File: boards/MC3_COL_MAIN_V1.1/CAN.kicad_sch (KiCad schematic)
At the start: 11 parts, among them J12 CAN, U8 TJA1051T/3

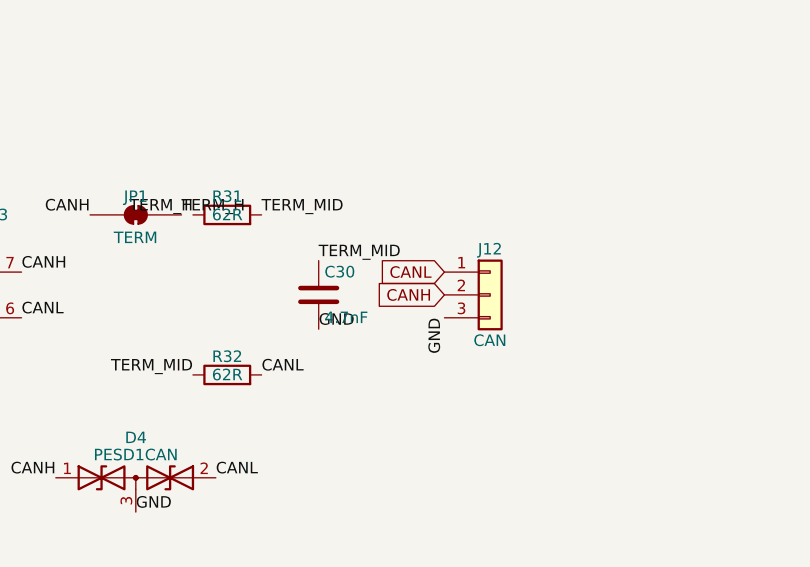
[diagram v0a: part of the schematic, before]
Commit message: V1.1: encoder FFC VIN on filtered VSENS, motor pads off MotorChannel, yaw nets renamed
- Connectors: encoder FFC VIN now fed from VSENS (VM through FB61 + C63);
  ENC_leaf1-4 / RC_OUT labels re-placed; SIG pull-ups to +3V3 noted on sheet
- MotorChannel: J7-J9 MOTOR pad connectors (Conn_01x02) and their OUT1/OUT2
  hierarchical labels removed from the shared sheet
- MCU: ENC_leaf1-4 global labels re-placed; sheet notes carried over
- Root: H5 SLOT-PASSTHRU mounting hole removed
- PCB: yaw motor nets YAW_OUT* -> /yaw/OUT*; CANH/CANL pad assignment swapped;
  VSENS/VM net reassignments and follow-up routing (~106 segments, 12 vias,
  zone edits) to match the schematic

Co-Authored-By: Claude Fable 5 <noreply@anthropic.com>
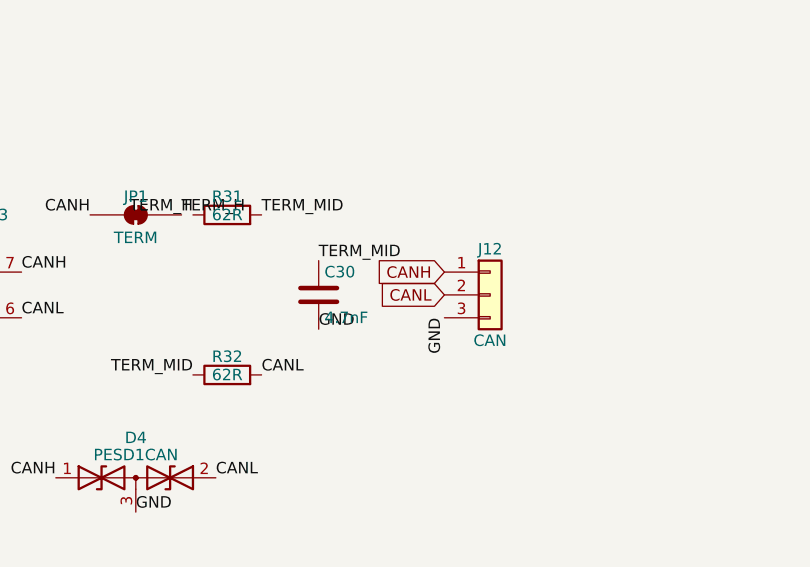
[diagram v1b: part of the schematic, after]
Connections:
- net CANH: now also J12.1 (Pin_1); no longer J12.2 (Pin_2)
- net CANL: now also J12.2 (Pin_2); no longer J12.1 (Pin_1)
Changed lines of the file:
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@@
 		)
 	)
-	(global_label "CANL"
+	(global_label "CANH"
 		(shape input)
 		(at 160.02 77.47 180)
@@
 		)
 	)
-	(global_label "CANH"
+	(global_label "CANL"
 		(shape input)
 		(at 160.02 80.01 180)

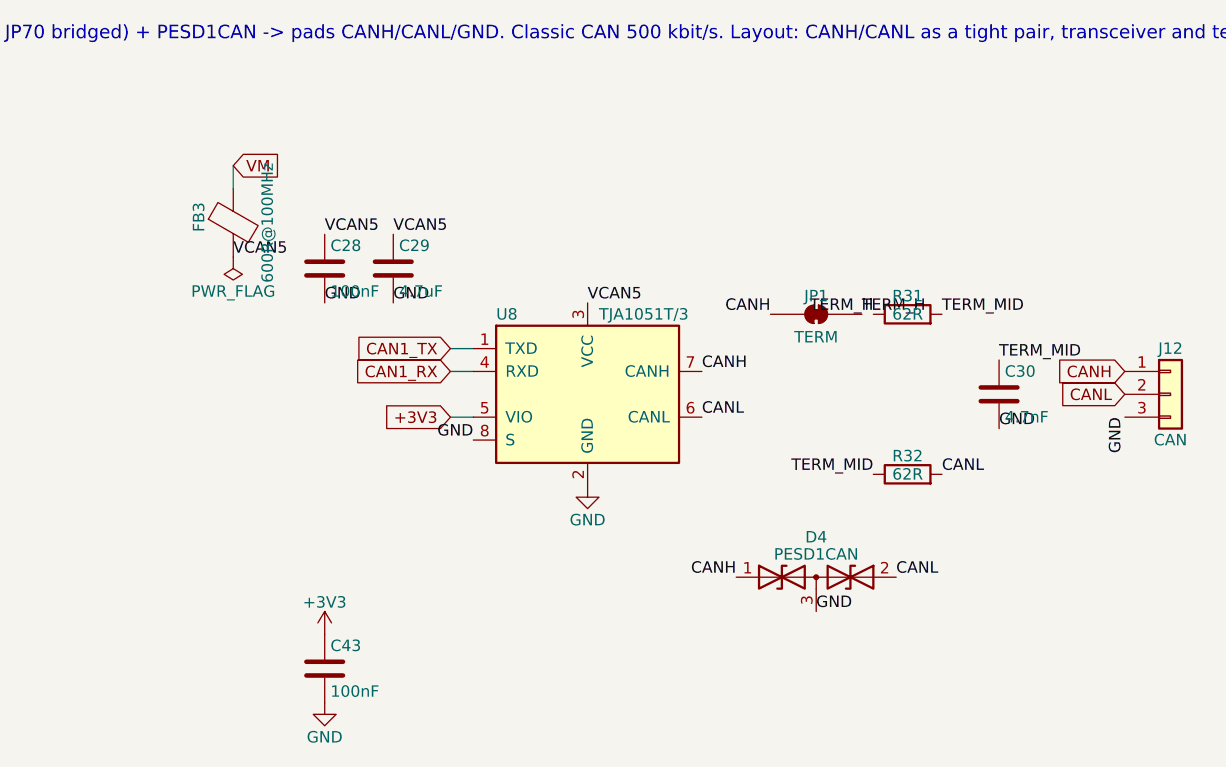
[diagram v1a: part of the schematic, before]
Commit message: Vault consolidation: Main-Board-02 rung folded back into Main-Board-01
Nothing was built at V1.0, so the 24 V revision never justified a rung bump.
Main-Board-01 now builds boards/MC3_COL_MAIN_V1.1 (24 V input); V1.0 stays in
the repo as the 5 V-only fallback revision. Repo side: CLAUDE.md rung mapping,
MIGRATION.md header and §14 pointer, LM61460 layout-note link. Vault side
(edited directly): Main-Board-01 Power rewritten as the 24 V chain, rung page
carries the V1.0→V1.1 delta/BOM/gates, Main-Board-02 folder deleted, 13 pages'
references rewritten.

Co-Authored-By: Claude Fable 5 <noreply@anthropic.com>
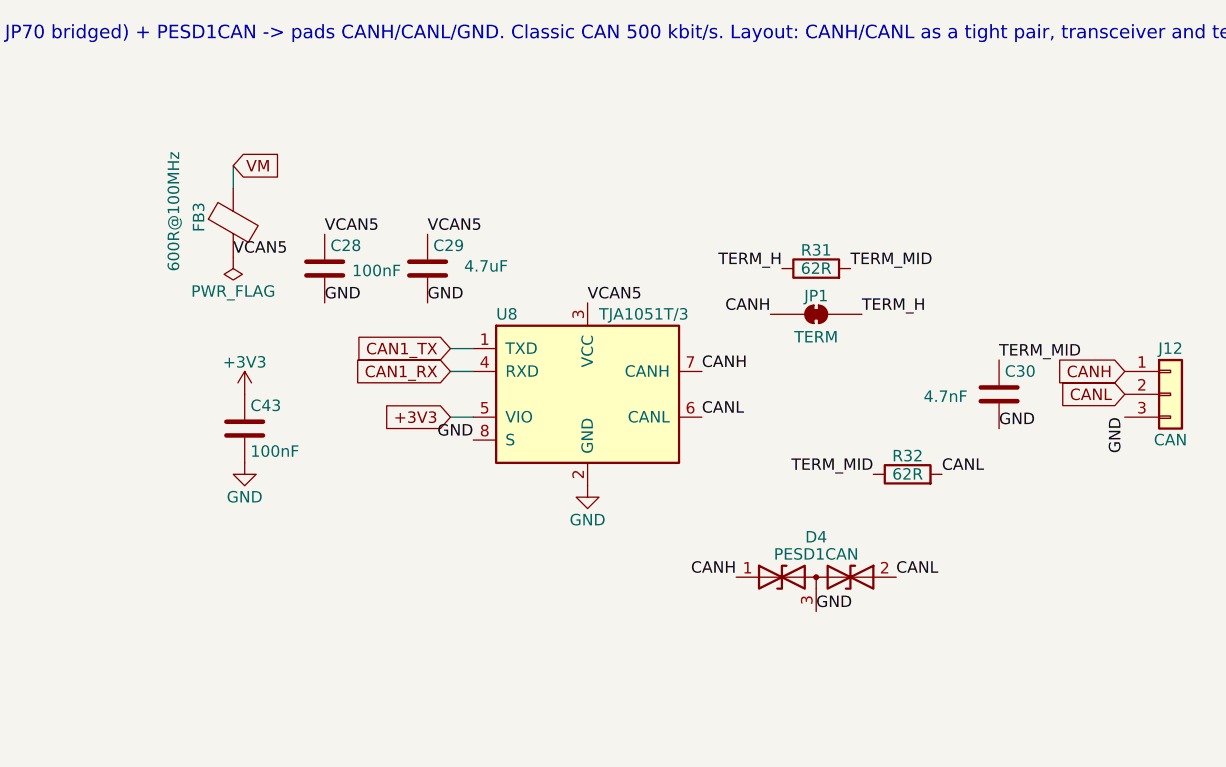
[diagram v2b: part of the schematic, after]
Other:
- moved on the sheet: C29, C43, R31
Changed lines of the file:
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@@
 	)
 	(label "TERM_MID"
-		(at 139.7 71.12 0)
+		(at 129.54 66.04 0)
 		(effects
 			(font
@@
 	)
 	(label "GND"
-		(at 78.74 69.85 0)
+		(at 82.55 69.85 0)
 		(effects
 			(font
@@
 	)
 	(label "TERM_H"
-		(at 132.08 71.12 180)
+		(at 121.92 66.04 180)
 		(effects
 			(font
@@
 	)
 	(label "VCAN5"
-		(at 78.74 62.23 0)
+		(at 82.55 62.23 0)
 		(effects
 			(font
@@
 	(symbol
 		(lib_id "power:+3V3")
-		(at 71.12 106.68 0)
+		(at 62.23 80.01 0)
 		(unit 1)
 		(body_style 1)
@@
 		(dnp no)
 		(property "Reference" "#PWR0120"
-			(at 71.12 110.49 0)
+			(at 62.23 83.82 0)
 			(hide yes)
 			(show_name no)
@@
 		)
 		(property "Value" "+3V3"
-			(at 71.12 103.124 0)
+			(at 62.23 76.454 0)
 			(show_name no)
 			(do_not_autoplace no)
@@
 		)
 		(property "Footprint" ""
-			(at 71.12 106.68 0)
+			(at 62.23 80.01 0)
 			(hide yes)
 			(show_name no)
@@
 		)
 		(property "Datasheet" ""
-			(at 71.12 106.68 0)
+			(at 62.23 80.01 0)
 			(hide yes)
 			(show_name no)
@@
 		)
 		(property "Description" ""
-			(at 71.12 106.68 0)
+			(at 62.23 80.01 0)
 			(show_name no)
 			(do_not_autoplace no)
@@
 		)
 		(property "Value" "100nF"
-			(at 71.755 68.58 0)
+			(at 74.168 66.294 0)
 			(show_name no)
 			(do_not_autoplace no)
@@
 	(symbol
 		(lib_id "Device:C")
-		(at 78.74 66.04 0)
+		(at 82.55 66.04 0)
 		(unit 1)
 		(body_style 1)
@@
 		(dnp no)
 		(property "Reference" "C29"
-			(at 79.375 63.5 0)
+			(at 83.185 63.5 0)
 			(show_name no)
 			(do_not_autoplace no)
@@
 		)
 		(property "Value" "4.7uF"
-			(at 79.375 68.58 0)
+			(at 86.614 65.786 0)
 			(show_name no)
 			(do_not_autoplace no)
@@
 		)
 		(property "Footprint" "MC3_COL_MAIN:C_0603_1608Metric"
-			(at 78.74 66.04 0)
+			(at 82.55 66.04 0)
 			(hide yes)
 			(show_name no)
@@
 		)
 		(property "Datasheet" ""
-			(at 78.74 66.04 0)
+			(at 82.55 66.04 0)
 			(hide yes)
 			(show_name no)
@@
 		)
 		(property "Description" ""
-			(at 78.74 66.04 0)
+			(at 82.55 66.04 0)
 			(show_name no)
 			(do_not_autoplace no)
@@
 		)
 		(property "LCSC" "C19666"
-			(at 78.74 66.04 0)
+			(at 82.55 66.04 0)
 			(hide yes)
 			(show_name no)
@@
 		)
 		(property "MPN" "CL10A475KO8NNNC"
-			(at 78.74 66.04 0)
+			(at 82.55 66.04 0)
 			(hide yes)
 			(show_name no)
@@
 	(symbol
 		(lib_id "power:GND")
-		(at 71.12 114.3 0)
+		(at 62.23 87.63 0)
 		(unit 1)
 		(body_style 1)
@@
 		(dnp no)
 		(property "Reference" "#PWR0121"
-			(at 71.12 120.65 0)
+			(at 62.23 93.98 0)
 			(hide yes)
 			(show_name no)
@@
 		)
 		(property "Value" "GND"
-			(at 71.12 118.11 0)
+			(at 62.23 91.44 0)
 			(show_name no)
 			(do_not_autoplace no)
@@
 		)
 		(property "Footprint" ""
-			(at 71.12 114.3 0)
+			(at 62.23 87.63 0)
 			(hide yes)
 			(show_name no)
@@
 		)
 		(property "Datasheet" ""
-			(at 71.12 114.3 0)
+			(at 62.23 87.63 0)
 			(hide yes)
 			(show_name no)
@@
 		)
 		(property "Description" ""
-			(at 71.12 114.3 0)
+			(at 62.23 87.63 0)
 			(show_name no)
 			(do_not_autoplace no)
@@
 	(symbol
 		(lib_id "Device:C")
-		(at 71.12 110.49 0)
+		(at 62.23 83.82 0)
 		(unit 1)
 		(body_style 1)
@@
 		(dnp no)
 		(property "Reference" "C43"
-			(at 71.755 107.95 0)
+			(at 62.865 81.28 0)
 			(show_name no)
 			(do_not_autoplace no)
@@
 		)
 		(property "Value" "100nF"
-			(at 71.755 113.03 0)
+			(at 62.865 86.36 0)
 			(show_name no)
 			(do_not_autoplace no)
@@
 		)
 		(property "Footprint" "MC3_COL_MAIN:C_0402_1005Metric"
-			(at 71.12 110.49 0)
+			(at 62.23 83.82 0)
 			(hide yes)
 			(show_name no)
@@
 		)
 		(property "Datasheet" ""
-			(at 71.12 110.49 0)
+			(at 62.23 83.82 0)
 			(hide yes)
 			(show_name no)
@@
 		)
 		(property "Description" ""
-			(at 71.12 110.49 0)
+			(at 62.23 83.82 0)
 			(show_name no)
 			(do_not_autoplace no)
@@
 		)
 		(property "LCSC" "C1525"
-			(at 71.12 110.49 0)
+			(at 62.23 83.82 0)
 			(hide yes)
 			(show_name no)
@@
 		)
 		(property "Note" "U8 VIO (pin 5) local decoupling - place within 4 mm of pin 5; wire pin1 to +3V3, pin2 to GND"
-			(at 71.12 110.49 0)
+			(at 62.23 83.82 0)
 			(hide yes)
 			(show_name no)
@@
 		)
 		(property "Value" "600R@100MHz"
-			(at 64.77 60.96 90)
+			(at 54.356 59.69 90)
 			(show_name no)
 			(do_not_autoplace no)
@@
 	(symbol
 		(lib_id "Device:R")
-		(at 135.89 71.12 90)
+		(at 125.73 66.04 90)
 		(unit 1)
 		(body_style 1)
@@
 		(dnp no)
 		(property "Reference" "R31"
-			(at 135.89 69.088 90)
+			(at 125.73 64.008 90)
 			(show_name no)
 			(do_not_autoplace no)
@@
 		)
 		(property "Value" "62R"
-			(at 135.89 71.12 90)
+			(at 125.73 66.04 90)
 			(show_name no)
 			(do_not_autoplace no)
@@
 		)
 		(property "Footprint" "MC3_COL_MAIN:R_0402_1005Metric"
-			(at 135.89 71.12 0)
+			(at 125.73 66.04 0)
 			(hide yes)
 			(show_name no)
@@
 		)
 		(property "Datasheet" ""
-			(at 135.89 71.12 0)
+			(at 125.73 66.04 0)
 			(hide yes)
 			(show_name no)
@@
 		)
 		(property "Description" ""
-			(at 135.89 71.12 0)
+			(at 125.73 66.04 0)
 			(show_name no)
 			(do_not_autoplace no)
@@
 		)
 		(property "LCSC" "C4962"
-			(at 135.89 71.12 0)
+			(at 125.73 66.04 0)
 			(hide yes)
 			(show_name no)
@@
 		)
 		(property "MPN" "0402WGF620JTCE"
-			(at 135.89 71.12 0)
+			(at 125.73 66.04 0)
 			(hide yes)
 			(show_name no)
@@
 		)
 		(property "Note" "Split termination 62R+62R (~124R) with C72 4.7nF to GND; JP70 bridged = terminated (board is a bus end on the bench). Cut JP70 if the board sits mid-bus in the machine"
-			(at 135.89 71.12 0)
+			(at 125.73 66.04 0)
 			(hide yes)
 			(show_name no)
@@
 		)
 		(property "Value" "4.7nF"
-			(at 146.685 82.55 0)
-			(show_name no)
-			(do_not_autoplace no)
+			(at 137.668 80.264 0)
+			(show_name no)
+			(do_not_autoplace no)

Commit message: V1.1 schematics: per-instance Description fields on ~63 symbols
The component-docs Role source of record. Netlist unchanged, ERC 0.

Co-Authored-By: Claude Fable 5 <noreply@anthropic.com>
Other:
- note removed: "CAN - machine control link (decision 2026-08-22; vault Control Electronics open item). STM32F412 CAN1 (PA11 RX / PA12 TX) -> TJA1051T/3 -> split termination (2x62R + 4.7nF, solder-jumper JP70 bridged) + PESD1CAN -> pads CANH/CANL/GND. Classic CAN 500 kbit/s. Layout: CANH/CANL as a tight pair, transceiver and termination next to the pads, D70 nearest the pads."
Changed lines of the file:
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@@
 	(generator_version "10.0")
 	(paper "A4")
-	(text "CAN - machine control link (decision 2026-08-22; vault Control Electronics open item). STM32F412 CAN1 (PA11 RX / PA12 TX) -> TJA1051T/3 -> split termination (2x62R + 4.7nF, solder-jumper JP70 bridged) + PESD1CAN -> pads CANH/CANL/GND. Classic CAN 500 kbit/s. Layout: CANH/CANL as a tight pair, transceiver and termination next to the pads, D70 nearest the pads."
-		(exclude_from_sim no)
-		(at 30 40 0)
-		(effects
-			(font
-				(size 1.5 1.5)
-			)
-		)
-	)
 	(wire
 		(pts
@@
 			)
 		)
-		(property "Description" ""
+		(property "Description" "CAN split termination, low side (62 Ω) — TERM_MID→CANL."
 			(at 135.89 88.9 0)
 			(show_name no)
@@
 			)
 		)
-		(property "Description" ""
+		(property "Description" "Machine CAN bare pads (CANH/CANL/GND), underside — kept as the fallback to J13."
 			(at 165.1 80.01 0)
 			(show_name no)
@@
 			)
 		)
-		(property "Description" ""
+		(property "Description" "CAN ESD clamp PESD1CAN at the bus pads."
 			(at 125.73 100.33 0)
 			(show_name no)
@@
 			)
 		)
-		(property "Description" ""
+		(property "Description" "CAN termination enable — bridged solder jumper (bridged = this node is a bus end)."
 			(at 125.73 71.12 0)
 			(show_name no)
@@
 			)
 		)
-		(property "Description" ""
+		(property "Description" "CAN split termination, high side (62 Ω) — behind JP1; CANH→TERM_MID."
 			(at 125.73 66.04 0)
 			(show_name no)
@@
 			)
 		)
-		(property "Description" ""
+		(property "Description" "CAN termination centre cap (common-mode drain) on TERM_MID."
 			(at 146.05 80.01 0)
 			(show_name no)
@@
 			)
 		)
-		(property "Description" ""
+		(property "Description" "CAN transceiver [[COL-COTS-0030]] TJA1051T/3: 5 V VCAN5 supply, 3.3 V VIO."
 			(at 100.33 80.01 0)
 			(show_name no)
